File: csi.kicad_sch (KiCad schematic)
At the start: 23 parts, among them J8 Conn_FFC_WE_68712614522_ONE-S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, U11 AP22615A_TSOT26, U12 AP22615A_TSOT26, U13 NTS0102_XSON

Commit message: [#54437] Clean CSI connections schematic
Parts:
- removed C59, C60: C_100n_0402, antmicro-footprints:C_0402_1005Metric, symbol antmicroCapacitors0402:C_100n_0402
- removed R101: R_4x0R_0201_array, antmicro-footprints:R_Array_4x0201_Panasonic_EXB18V, symbol antmicroResistorNetworksArrays:R_4x0R_0201_array
- removed R91, R92: R_0R_0402, antmicro-footprints:R_0402_1005Metric, symbol antmicroResistors0402:R_0R_0402
- removed R93: R_4x2k2_0201_array, antmicro-footprints:R_Array_4x0201_Panasonic_EXB18V, symbol antmicroResistorNetworksArrays:R_4x2k2_0201_array
- removed R94: R_10k_0402, antmicro-footprints:R_0402_1005Metric, symbol antmicroResistors0402:R_10k_0402
- removed U13: NTS0102_XSON, antmicro-footprints:XSON-8_1x1.95mm_P0.5mm, symbol antmicroLogicTranslatorsLevelShifters:NTS0102_XSON
- added R?: R_10k_0402, antmicro-footprints:R_0402_1005Metric, symbol antmicroResistors0402:R_10k_0402
- added TP? (x2): TP_0.75mm_SMD, antmicro-footprints:TP_SMD_0.75mm, symbol antmicroTestPoints:TP_0.75mm_SMD
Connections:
- net +3V3: now also R?.1; no longer R96.1
- net +5V: now also R96.1
- net I_{2}C_CSI0.SCL: now also J8.40
- net I_{2}C_CSI0.SDA: now also J8.39
- net I_{2}C_CSI1.SCL: now also J8.42
- net I_{2}C_CSI1.SDA: now also J8.41
- net CSIA_3V3 renamed CSI_3V3
- net CSIA_3V3_ISET: no longer names the net of R98.2, U12.5 (ISET)
- net CSIA_5V renamed CSI_5V
- net CSIA_5V_ISET: no longer names the net of R97.2, U11.5 (ISET)
- net CSIA_FLG: no longer names the net of R96.2, U11.3 (FLG)
- net CSIA_FLG: now also TP?.1; no longer U12.3 (FLG)
- net CSIA_PEN renamed CamCtrl.EN
- net VSYNC_CAM0_3V3 renamed CamCtrl.VSYNC0
- net VSYNC_CAM1_3V3 renamed CamCtrl.VSYNC1
- new net: R?.2, TP?.1, U12.3 (FLG)
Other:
- note added: "Both switches set to 1.5A current limit"
- note added: "CSI connector"
- note added: "Power switches"
- note removed: "ALL SWITCHES 1.5A CURRENT LIMIT"
- note removed: "CSI connector J7"
- note removed: "Level shifter"
- note removed: "Power switch"
- moved on the sheet: C55, C56, C57, C58, D16, D17, J8, R100, R95, R96, R97, R98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

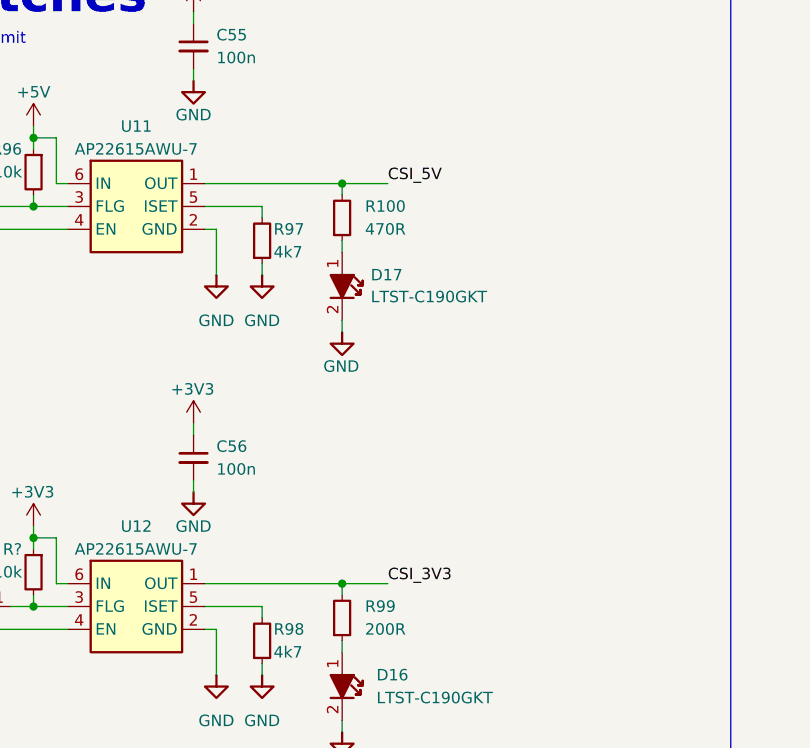
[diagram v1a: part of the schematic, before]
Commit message: [#54617] Clean labels: align & reduce duplicates
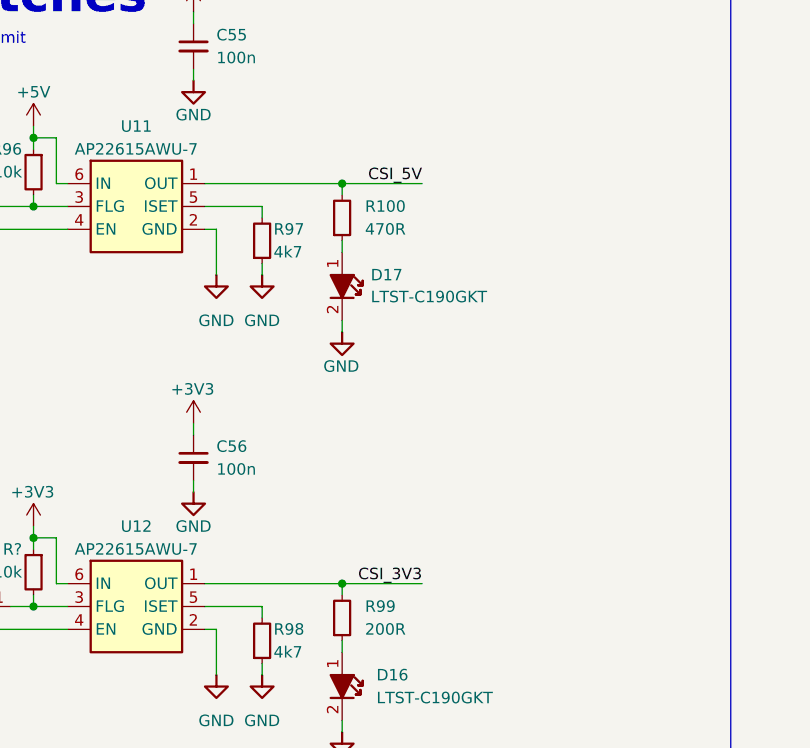
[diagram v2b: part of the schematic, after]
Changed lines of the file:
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@@
     (stroke (width 0) (type default) (color 0 0 0 0))
   )
-  (wire (pts (xy 152.4 129.54) (xy 157.48 129.54))
+  (wire (pts (xy 152.4 129.54) (xy 161.29 129.54))
     (stroke (width 0) (type default) (color 0 0 0 0))
   )
@@
     (stroke (width 0) (type default) (color 0 0 0 0))
   )
-  (wire (pts (xy 152.4 173.99) (xy 157.48 173.99))
+  (wire (pts (xy 152.4 173.99) (xy 161.29 173.99))
     (stroke (width 0) (type default) (color 0 0 0 0))
   )
@@
     (effects (font (size 1.27 1.27)) (justify left bottom))
   )
-  (label "CSI_3V3" (at 157.48 173.99 0)
-    (effects (font (size 1.27 1.27)) (justify left bottom))
+  (label "CSI_3V3" (at 161.29 173.99 180)
+    (effects (font (size 1.27 1.27)) (justify right bottom))
   )
   (label "CamCtrl.VSYNC0" (at 299.72 140.97 0)
@@
     (effects (font (size 1.27 1.27)) (justify left bottom))
   )
-  (label "CSI_5V" (at 157.48 129.54 0)
-    (effects (font (size 1.27 1.27)) (justify left bottom))
+  (label "CSI_5V" (at 161.29 129.54 180)
+    (effects (font (size 1.27 1.27)) (justify right bottom))
   )
   (label "CSI1.CLK_N" (at 299.72 130.81 0)

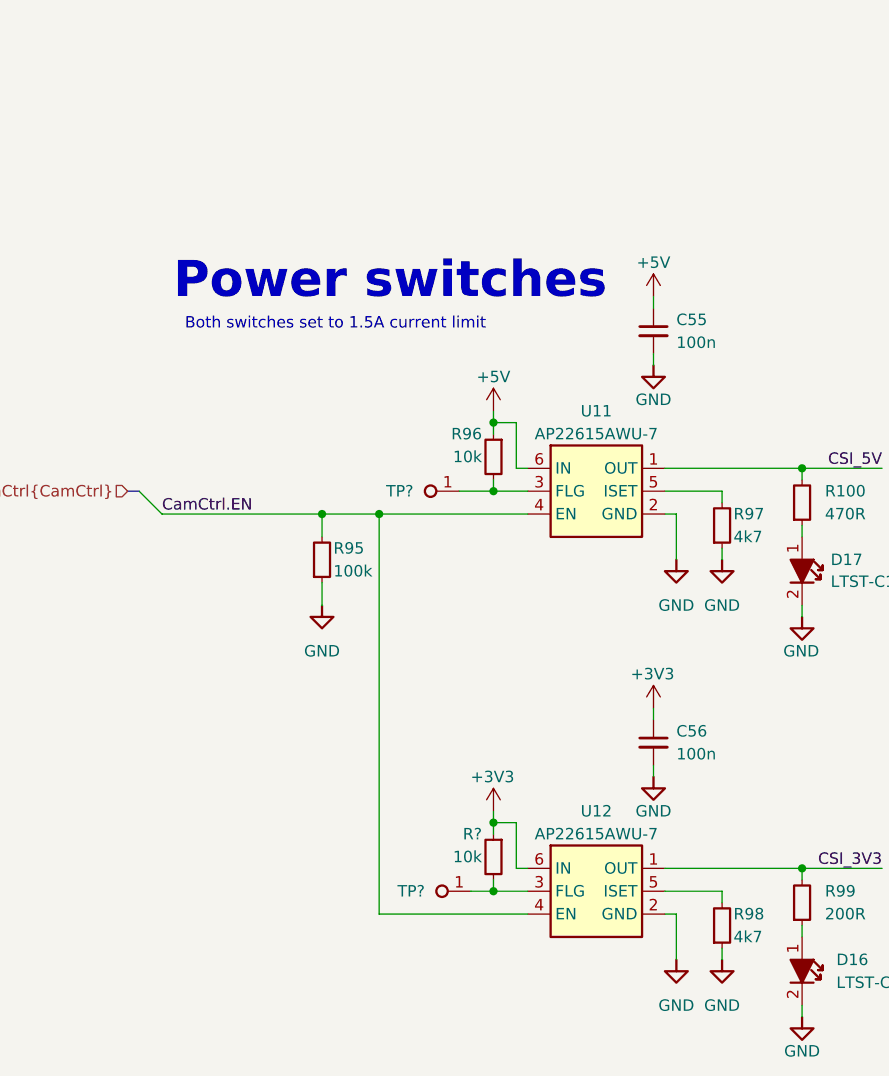
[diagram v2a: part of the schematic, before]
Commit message: [#54617] Change how CSI switches decoupling capacitors are placed on schematic
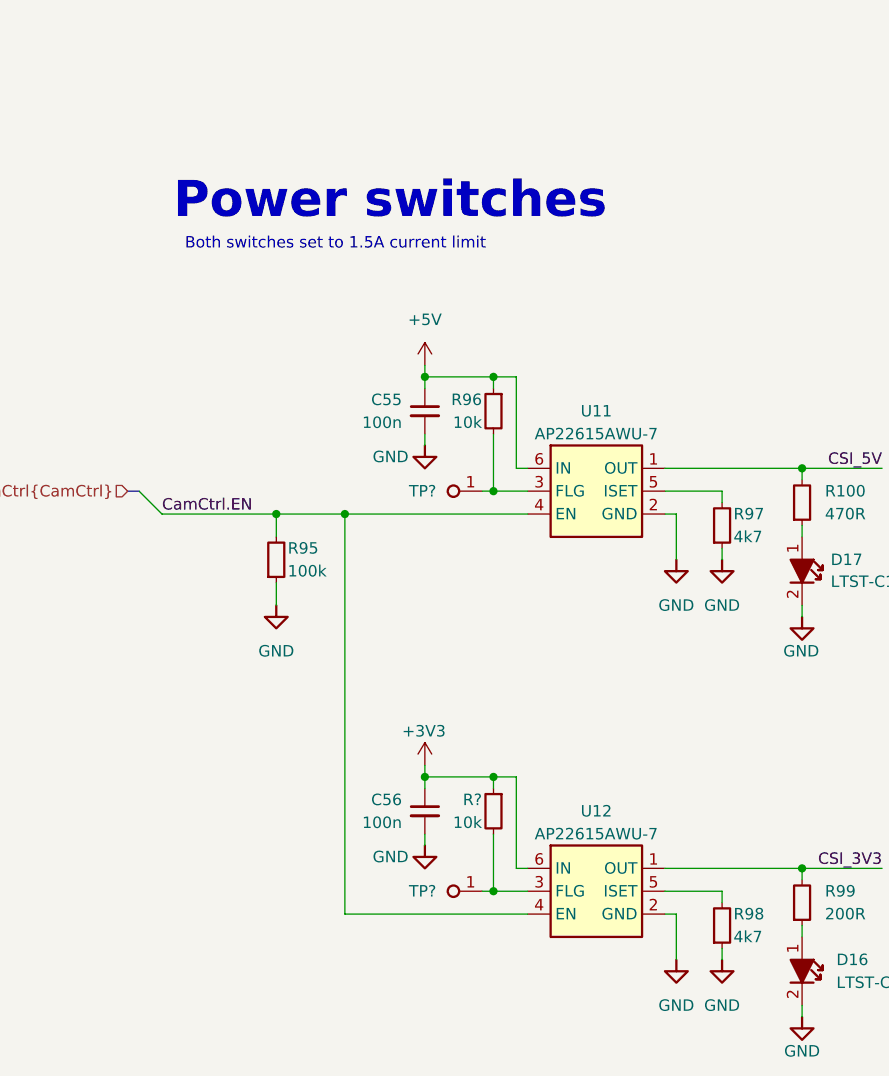
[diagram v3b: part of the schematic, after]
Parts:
- removed TP? (x2): TP_0.75mm_SMD, antmicro-footprints:TP_SMD_0.75mm, symbol antmicroTestPoints:TP_0.75mm_SMD
- added TP? (x2): TP_0.75mm_SMD, antmicro-footprints:TP_SMD_0.75mm, symbol antmicroTestPoints:TP_0.75mm_SMD
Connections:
- net at R?.2, U12.3 (FLG): now also TP?.1
- net at R96.2, U11.3 (FLG): now also TP?.1
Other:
- moved on the sheet: C55, C56, R95, R96, R?

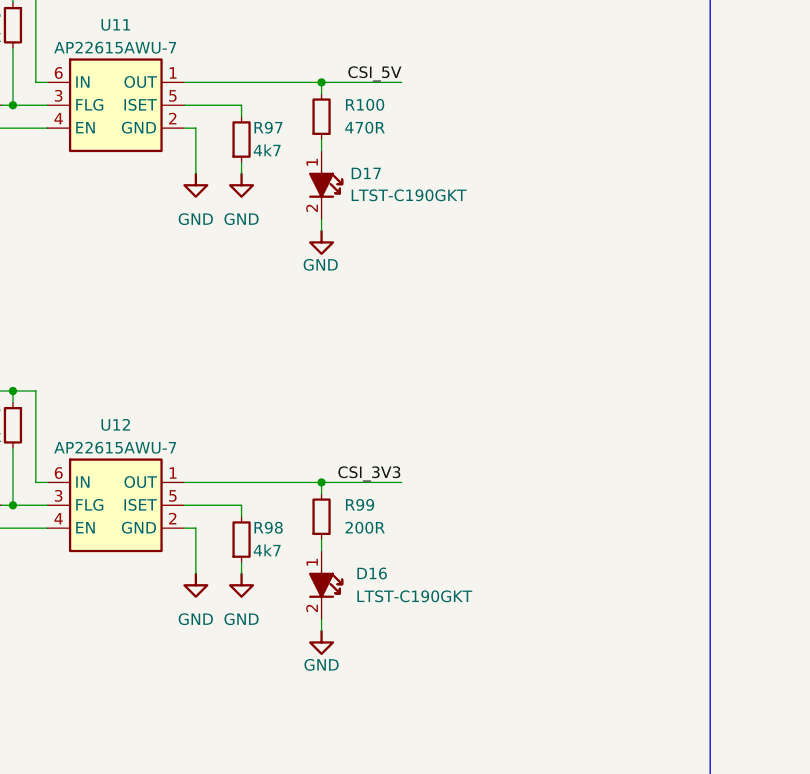
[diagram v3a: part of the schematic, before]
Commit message: [#54617] Uniform diodes MPN
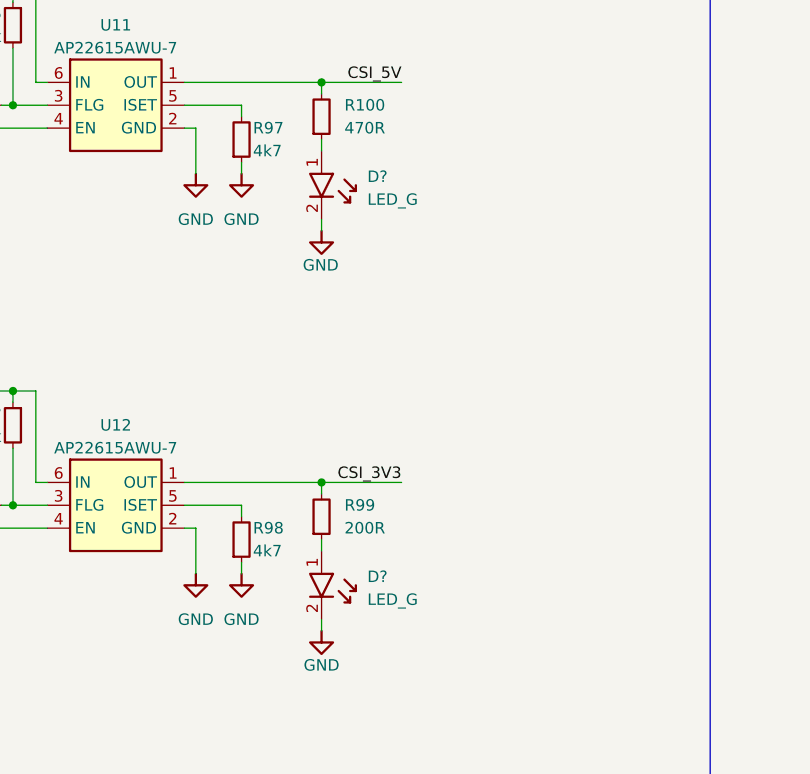
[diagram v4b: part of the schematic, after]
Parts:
- removed D16, D17: LED_G_0603_LTST-C190GKT, antmicro-footprints:LED_0603_1608Metric_G, symbol antmicroLEDIndicationDiscrete:LED_G_0603_LTST-C190GKT
- added D? (x2): LED_G, antmicro-footprints:LED_0603_1608Metric_R, symbol antmicroLEDIndicationDiscrete:LED_R_0603_598-8D80-107F
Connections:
- net GND: now also D?.2, D?.2
- net at R99.1: now also D?.1
- net at R100.1: now also D?.1
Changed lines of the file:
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@@
     (pin "2")
   )
-  (symbol (lib_id "antmicroLEDIndicationDiscrete:LED_G_0603_LTST-C190GKT") (at 152.4 181.61 270) (unit 1)
-    (in_bom yes) (on_board yes) (fields_autoplaced)
-    (property "Reference" "D16" (id 0) (at 156.21 184.1499 90)
-      (effects (font (size 1.27 1.27)) (justify left))
-    )
-    (property "Value" "LED_G_0603_LTST-C190GKT" (id 1) (at 149.86 186.6899 90)
-      (effects (font (size 1.27 1.27) (thickness 0.15)) (justify right) hide)
-    )
-    (property "Footprint" "antmicro-footprints:LED_0603_1608Metric_G" (id 2) (at 142.24 204.47 0)
-      (effects (font (size 1.27 1.27) (thickness 0.15)) (justify left bottom) hide)
-    )
-    (property "Datasheet" "https://media.digikey.com/pdf/Data%20Sheets/Lite-On%20PDFs/LTST-C190GKT.pdf" (id 3) (at 139.7 204.47 0)
-      (effects (font (size 1.27 1.27) (thickness 0.15)) (justify left bottom) hide)
-    )
-    (property "MPN" "LTST-C190GKT" (id 4) (at 156.21 186.6899 90)
-      (effects (font (size 1.27 1.27) (thickness 0.15)) (justify left))
-    )
-    (property "Manufacturer" "Lite-On Inc." (id 5) (at 134.62 204.47 0)
-      (effects (font (size 1.27 1.27) (thickness 0.15)) (justify left bottom) hide)
-    )
-    (property "Author" "Antmicro" (id 6) (at 132.08 204.47 0)
-      (effects (font (size 1.27 1.27) (thickness 0.15)) (justify left bottom) hide)
-    )
-    (property "License" "Apache-2.0" (id 7) (at 129.54 204.47 0)
+  (symbol (lib_id "antmicroLEDIndicationDiscrete:LED_R_0603_598-8D80-107F") (at 152.4 181.61 270) (unit 1)
+    (in_bom yes) (on_board yes) (fields_autoplaced)
+    (property "Reference" "D?" (id 0) (at 157.48 184.4674 90)
+      (effects (font (size 1.27 1.27) (thickness 0.15)) (justify left))
+    )
+    (property "Value" "LED_G" (id 1) (at 157.48 187.0074 90)
+      (effects (font (size 1.27 1.27) (thickness 0.15)) (justify left))
+    )
+    (property "Footprint" "antmicro-footprints:LED_0603_1608Metric_R" (id 2) (at 144.78 204.47 0)
+      (effects (font (size 1.27 1.27) (thickness 0.15)) (justify left bottom) hide)
+    )
+    (property "Datasheet" "https://www.farnell.com/datasheets/3093797.pdf" (id 3) (at 142.24 204.47 0)
+      (effects (font (size 1.27 1.27) (thickness 0.15)) (justify left bottom) hide)
+    )
+    (property "MPN" "598-8D80-107F" (id 4) (at 157.48 187.0074 90)
+      (effects (font (size 1.27 1.27) (thickness 0.15)) (justify left) hide)
+    )
+    (property "Manufacturer" "Dialight" (id 5) (at 137.16 204.47 0)
+      (effects (font (size 1.27 1.27) (thickness 0.15)) (justify left bottom) hide)
+    )
+    (property "Author" "Antmicro" (id 6) (at 134.62 204.47 0)
+      (effects (font (size 1.27 1.27) (thickness 0.15)) (justify left bottom) hide)
+    )
+    (property "License" "Apache-2.0" (id 7) (at 132.08 204.47 0)
       (effects (font (size 1.27 1.27) (thickness 0.15)) (justify left bottom) hide)
     )
@@
     (pin "2")
   )
-  (symbol (lib_id "antmicroLEDIndicationDiscrete:LED_G_0603_LTST-C190GKT") (at 152.4 137.16 270) (unit 1)
-    (in_bom yes) (on_board yes)
-    (property "Reference" "D17" (id 0) (at 155.575 139.7 90)
-      (effects (font (size 1.27 1.27)) (justify left))
-    )
-    (property "Value" "LED_G_0603_LTST-C190GKT" (id 1) (at 156.21 142.2399 90)
+  (symbol (lib_id "antmicroLEDIndicationDiscrete:LED_R_0603_598-8D80-107F") (at 152.4 137.16 270) (unit 1)
+    (in_bom yes) (on_board yes) (fields_autoplaced)
+    (property "Reference" "D?" (id 0) (at 157.48 140.0174 90)
+      (effects (font (size 1.27 1.27) (thickness 0.15)) (justify left))
+    )
+    (property "Value" "LED_G" (id 1) (at 157.48 142.5574 90)
+      (effects (font (size 1.27 1.27) (thickness 0.15)) (justify left))
+    )
+    (property "Footprint" "antmicro-footprints:LED_0603_1608Metric_R" (id 2) (at 144.78 160.02 0)
+      (effects (font (size 1.27 1.27) (thickness 0.15)) (justify left bottom) hide)
+    )
+    (property "Datasheet" "https://www.farnell.com/datasheets/3093797.pdf" (id 3) (at 142.24 160.02 0)
+      (effects (font (size 1.27 1.27) (thickness 0.15)) (justify left bottom) hide)
+    )
+    (property "MPN" "598-8D80-107F" (id 4) (at 157.48 142.5574 90)
       (effects (font (size 1.27 1.27) (thickness 0.15)) (justify left) hide)
     )
-    (property "Footprint" "antmicro-footprints:LED_0603_1608Metric_G" (id 2) (at 142.24 160.02 0)
-      (effects (font (size 1.27 1.27) (thickness 0.15)) (justify left bottom) hide)
-    )
-    (property "Datasheet" "https://media.digikey.com/pdf/Data%20Sheets/Lite-On%20PDFs/LTST-C190GKT.pdf" (id 3) (at 139.7 160.02 0)
-      (effects (font (size 1.27 1.27) (thickness 0.15)) (justify left bottom) hide)
-    )
-    (property "MPN" "LTST-C190GKT" (id 4) (at 155.575 142.875 90)
-      (effects (font (size 1.27 1.27) (thickness 0.15)) (justify left bottom))
-    )
-    (property "Manufacturer" "Lite-On Inc." (id 5) (at 134.62 160.02 0)
-      (effects (font (size 1.27 1.27) (thickness 0.15)) (justify left bottom) hide)
-    )
-    (property "Author" "Antmicro" (id 6) (at 132.08 160.02 0)
-      (effects (font (size 1.27 1.27) (thickness 0.15)) (justify left bottom) hide)
-    )
-    (property "License" "Apache-2.0" (id 7) (at 129.54 160.02 0)
-      (effects (font (size 1.27 1.27) (thickness 0.15)) (justify left bottom) hide)
-    )
+    (property "Manufacturer" "Dialight" (id 5) (at 137.16 160.02 0)
+      (effects (font (size 1.27 1.27) (thickness 0.15)) (justify left bottom) hide)
+    )
+    (property "Author" "Antmicro" (id 6) (at 134.62 160.02 0)
+      (effects (font (size 1.27 1.27) (thickness 0.15)) (justify left bottom) hide)
+    )
+    (property "License" "Apache-2.0" (id 7) (at 132.08 160.02 0)
+      (effects (font (size 1.27 1.27) (thickness 0.15)) (justify left bottom) hide)
+    )
